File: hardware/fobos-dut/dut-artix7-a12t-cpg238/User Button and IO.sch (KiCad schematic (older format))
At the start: 26 parts, among them Q4 BSS138, Q5 BSS138, Q6 BSS138, Q7 BSS138

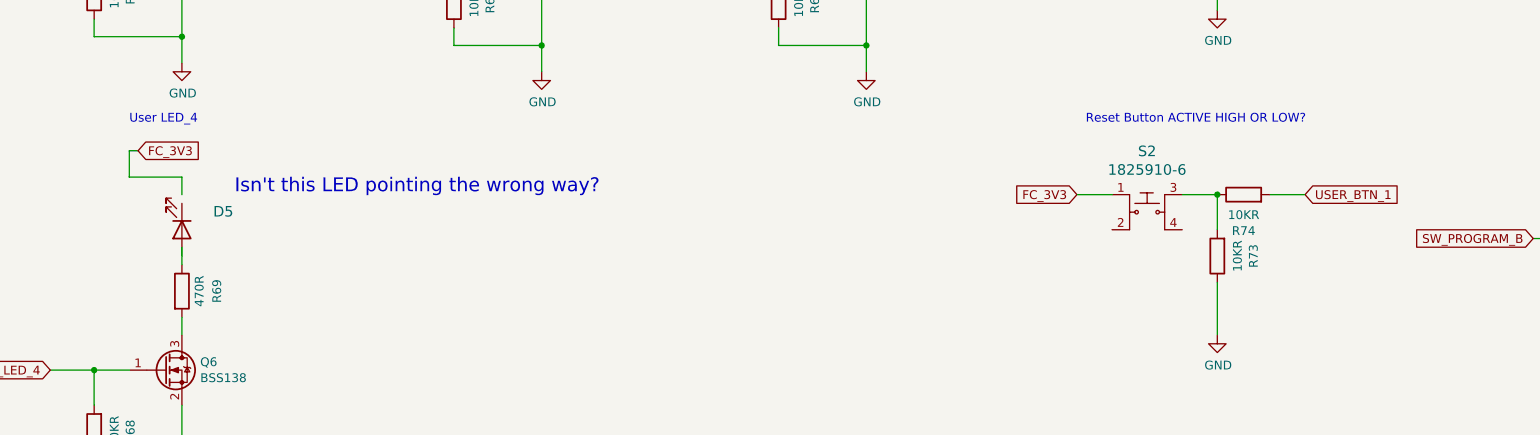
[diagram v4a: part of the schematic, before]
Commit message: placed user buttons and leds, flash
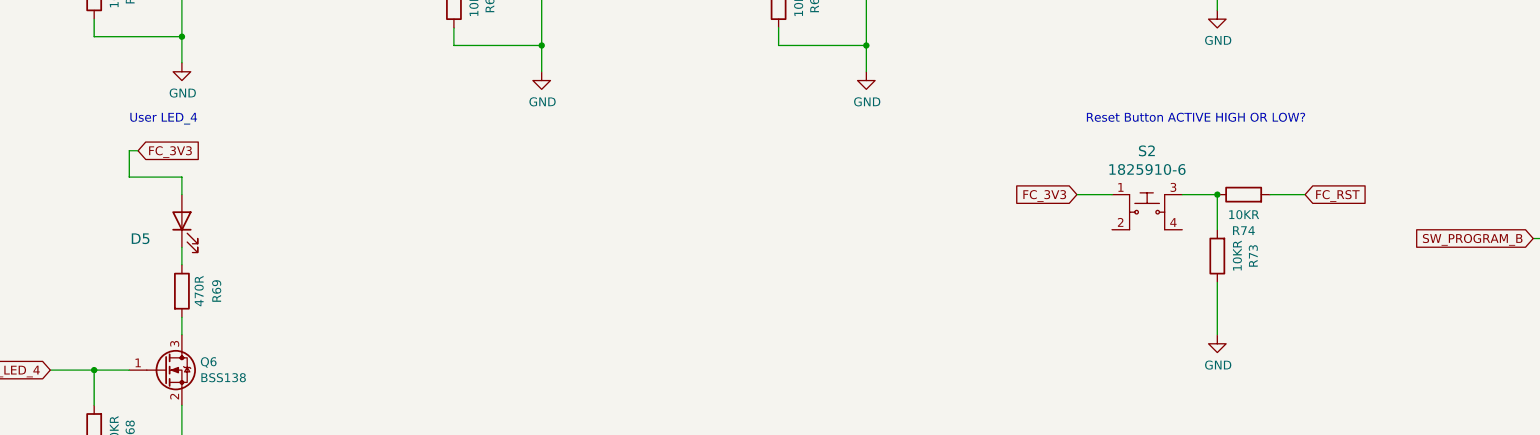
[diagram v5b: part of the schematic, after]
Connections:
- net FC_3V3: now also D5.2 (A)
- net USER_BTN_1: no longer R74.2
- net at D5.1 (K): now also R69.1
- new net FC_RST: R74.2
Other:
- note removed: "Isn't this LED pointing the wrong way?"
- moved on the sheet: D5
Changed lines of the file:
@@
 L Device:LED D?
 U 1 1 602D02FE
-P 2050 4750
+P 2050 4700
 AR Path="/5F449901/602D02FE" Ref="D?"  Part="1"
 AR Path="/600CE672/602D02FE" Ref="D5"  Part="1"
-F 0 "D5" V 1947 4928 60  0000 L CNN
-F 1 "LG_L29K-G2J1-24-Z" V 2053 4928 60  0001 L CNN
-F 2 "LED_SMD:LED_0603_1608Metric" H 2250 4950 60  0001 L CNN
-F 3 "https://dammedia.osram.info/media/resource/hires/osram-dam-2493945/LG%20L29K.pdf" H 2250 5050 60  0001 L CNN
-F 4 "475-2709-1-ND" H 2250 5150 60  0001 L CNN "Digi-Key_PN"
-F 5 "LG L29K-G2J1-24-Z" H 2250 5250 60  0001 L CNN "MPN"
-F 6 "Optoelectronics" H 2250 5350 60  0001 L CNN "Category"
-F 7 "LED Indication - Discrete" H 2250 5450 60  0001 L CNN "Family"
-F 8 "https://dammedia.osram.info/media/resource/hires/osram-dam-2493945/LG%20L29K.pdf" H 2250 5550 60  0001 L CNN "DK_Datasheet_Link"
-F 9 "/product-detail/en/osram-opto-semiconductors-inc/LG-L29K-G2J1-24-Z/475-2709-1-ND/1938876" H 2250 5650 60  0001 L CNN "DK_Detail_Page"
-F 10 "LED GREEN DIFFUSED 0603 SMD" H 2250 5750 60  0001 L CNN "Description"
-F 11 "OSRAM Opto Semiconductors Inc." H 2250 5850 60  0001 L CNN "Manufacturer"
-F 12 "Active" H 2250 5950 60  0001 L CNN "Status"
-	1    2050 4750
-	0    1    1    0
+F 0 "D5" V 1947 4878 60  0000 L CNN
+F 1 "LG_L29K-G2J1-24-Z" V 2053 4878 60  0001 L CNN
+F 2 "LED_SMD:LED_0603_1608Metric" H 2250 4900 60  0001 L CNN
+F 3 "https://dammedia.osram.info/media/resource/hires/osram-dam-2493945/LG%20L29K.pdf" H 2250 5000 60  0001 L CNN
+F 4 "475-2709-1-ND" H 2250 5100 60  0001 L CNN "Digi-Key_PN"
+F 5 "LG L29K-G2J1-24-Z" H 2250 5200 60  0001 L CNN "MPN"
+F 6 "Optoelectronics" H 2250 5300 60  0001 L CNN "Category"
+F 7 "LED Indication - Discrete" H 2250 5400 60  0001 L CNN "Family"
+F 8 "https://dammedia.osram.info/media/resource/hires/osram-dam-2493945/LG%20L29K.pdf" H 2250 5500 60  0001 L CNN "DK_Datasheet_Link"
+F 9 "/product-detail/en/osram-opto-semiconductors-inc/LG-L29K-G2J1-24-Z/475-2709-1-ND/1938876" H 2250 5600 60  0001 L CNN "DK_Detail_Page"
+F 10 "LED GREEN DIFFUSED 0603 SMD" H 2250 5700 60  0001 L CNN "Description"
+F 11 "OSRAM Opto Semiconductors Inc." H 2250 5800 60  0001 L CNN "Manufacturer"
+F 12 "Active" H 2250 5900 60  0001 L CNN "Status"
+	1    2050 4700
+	0    -1   -1   0
 $EndComp
 $Comp
@@
 Wire Wire Line
 	2050 5350 2050 5250
-Wire Wire Line
-	2050 4950 2050 4850
 Wire Wire Line
 	2050 4450 2050 4550
@@
 	7150 4550 7350 4550
 Text GLabel 8450 4550 2    50   Input ~ 0
-USER_BTN_1
+FC_RST
 Wire Wire Line
 	8450 4550 8250 4550
@@
 Text Notes 9800 4150 0    50   ~ 0
 Progam_B Button
-Text Notes 2350 4550 0    79   ~ 0
-Isn't this LED pointing the wrong way?
+Wire Wire Line
+	2050 4850 2050 4950
 $EndSCHEMATC
